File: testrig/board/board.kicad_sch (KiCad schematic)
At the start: 25 parts, among them J1 Conn_01x02_Male, SW1 SW_DIP_x04, U1 AMS1117-3.3, U2 XO2-DIP20, U3 74LVC574, U4 74LVC574, U5 74LVC574, U6 74LVC574, U7 74LVC574, U99 ZIF-40, X1 ASE-80MHz

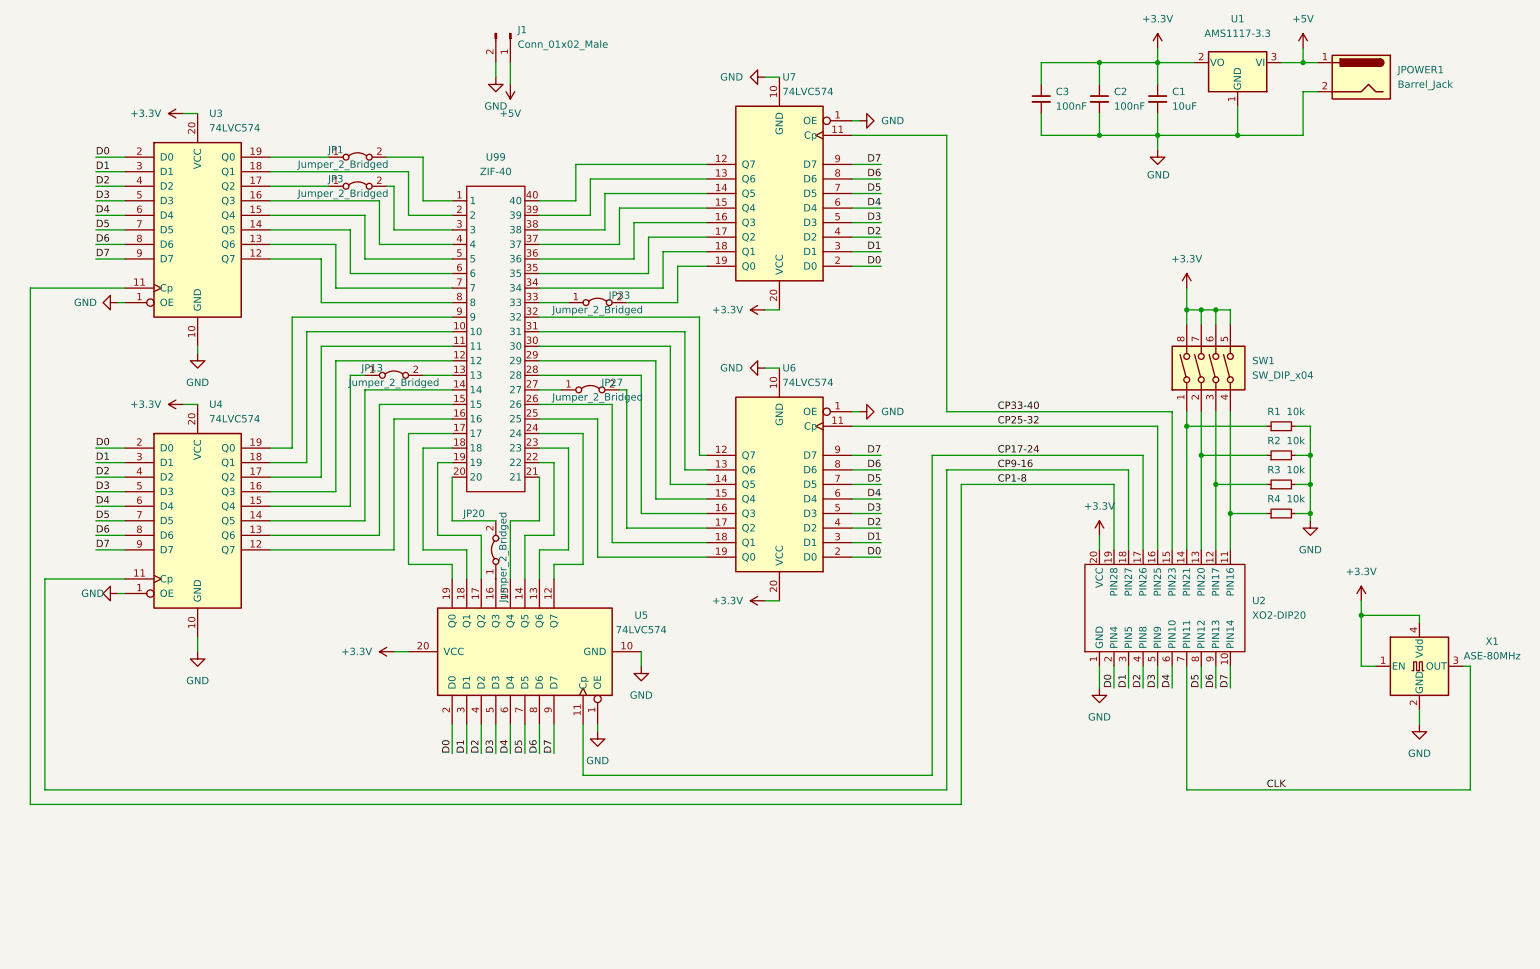
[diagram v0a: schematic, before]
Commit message: Test rig example code
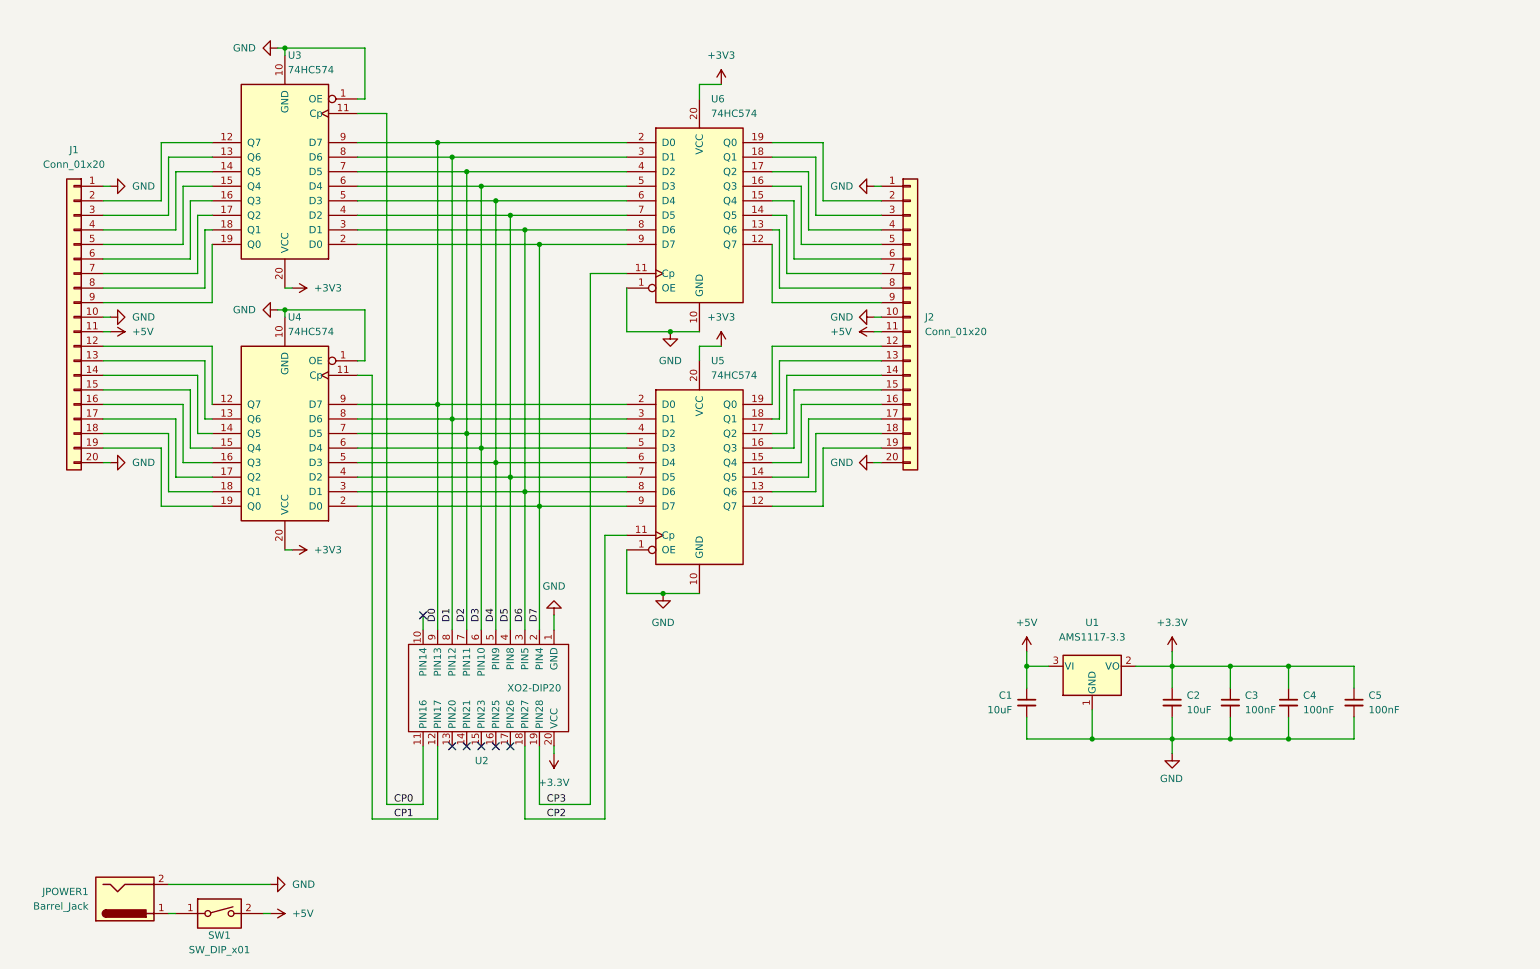
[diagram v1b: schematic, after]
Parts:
- removed J1: Conn_01x02_Male, symbol Connector:Conn_01x02_Male
- removed JP1, JP13, JP20, JP27, JP3, JP33: Jumper_2_Bridged, symbol Jumper:Jumper_2_Bridged
- removed R1, R2, R3, R4: 10k, symbol Device:R_Small
- removed SW1: SW_DIP_x04, symbol Switch:SW_DIP_x04
- removed U3, U4, U5, U6, U7: 74LVC574, symbol 74xx:74LS574
- removed U99: ZIF-40, symbol Library:ZIF-40
- removed X1: ASE-80MHz, Oscillator:Oscillator_SMD_Abracon_ASE-4Pin_3.2x2.5mm, symbol Oscillator:ASE-xxxMHz
- added C2: 10uF, symbol Device:C_Small
- added C5: 100nF, symbol Device:C_Small
- added J1, J2: Conn_01x20, symbol Connector_Generic:Conn_01x20
- added SW1: SW_DIP_x01, symbol Switch:SW_DIP_x01
- added U3, U4, U5, U6: 74HC574, symbol 74xx:74HCT574
- renumbered C2 to C3, C3 to C4
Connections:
- net CLK is gone; now on net D2: U2.7 (PIN11)
- net +3.3V: now also C2.1, C5.1; no longer C1.1
- net +5V: now also C1.1, J1.11 (Pin_11), J2.11 (Pin_11), SW1.2; no longer JPOWER1.1
- net D0: now also U2.9 (PIN13), U3.9 (D7), U4.9 (D7), U5.2 (D0), U6.2 (D0); no longer U2.2 (PIN4)
- net D1: now also U2.8 (PIN12), U3.8 (D6), U4.8 (D6), U5.3 (D1), U6.3 (D1); no longer U2.3 (PIN5)
- net D2: now also U3.7 (D5), U4.7 (D5), U5.4 (D2), U6.4 (D2); no longer U2.4 (PIN8)
- net D3: now also U2.6 (PIN10), U3.6 (D4), U4.6 (D4), U5.5 (D3), U6.5 (D3); no longer U2.5 (PIN9)
- net D4: now also U2.5 (PIN9), U3.5 (D3), U4.5 (D3), U5.6 (D4), U6.6 (D4); no longer U2.6 (PIN10)
- net D5: now also U2.4 (PIN8), U3.4 (D2), U4.4 (D2), U5.7 (D5), U6.7 (D5); no longer U2.8 (PIN12)
- net D6: now also U2.3 (PIN5), U3.3 (D1), U4.3 (D1), U5.8 (D6), U6.8 (D6); no longer U2.9 (PIN13)
- net D7: now also U2.2 (PIN4), U3.2 (D0), U4.2 (D0), U5.9 (D7), U6.9 (D7); no longer U2.10 (PIN14)
- net GND: now also C2.2, C5.2, J1.1 (Pin_1), J1.10 (Pin_10), J1.20 (Pin_20), J2.1 (Pin_1), J2.10 (Pin_10), J2.20 (Pin_20), U3.1 (OE), U3.10 (GND), U4.1 (OE), U4.10 (GND), U5.1 (OE), U5.10 (GND), U6.1 (OE), U6.10 (GND)
- net CP0: now reaches U2.11 (PIN16)
- net CP0: now also U3.11 (Cp)
- net CP1: now reaches U2.12 (PIN17)
- net CP1: now also U4.11 (Cp)
- net CP1-8 renamed CP3
- net CP3: now also U6.11 (Cp)
- net CP17-24: no longer names the net of U2.17 (PIN26)
- net CP25-32: no longer names the net of U2.16 (PIN25)
- net CP33-40: no longer names the net of U2.15 (PIN23)
- net CP9-16 renamed CP2
- net CP2: now also U5.11 (Cp)
- new net: J1.2 (Pin_2), U3.12 (Q7)
- new net: J1.3 (Pin_3), U3.13 (Q6)
- new net: J1.4 (Pin_4), U3.14 (Q5)
- new net: J1.5 (Pin_5), U3.15 (Q4)
- new net: J1.6 (Pin_6), U3.16 (Q3)
- new net: J1.7 (Pin_7), U3.17 (Q2)
- new net: J1.8 (Pin_8), U3.18 (Q1)
- new net: J1.9 (Pin_9), U3.19 (Q0)
- new net: J2.19 (Pin_19), U5.12 (Q7)
- new net: J2.18 (Pin_18), U5.13 (Q6)
- new net: J2.17 (Pin_17), U5.14 (Q5)
- new net: J2.16 (Pin_16), U5.15 (Q4)
- new net: J2.15 (Pin_15), U5.16 (Q3)
- new net: J2.14 (Pin_14), U5.17 (Q2)
- new net: J2.13 (Pin_13), U5.18 (Q1)
- new net: J2.12 (Pin_12), U5.19 (Q0)
- new net: J2.2 (Pin_2), U6.19 (Q0)
- new net: J2.3 (Pin_3), U6.18 (Q1)
- new net: J2.4 (Pin_4), U6.17 (Q2)
- new net: J2.5 (Pin_5), U6.16 (Q3)
- new net: J2.6 (Pin_6), U6.15 (Q4)
- new net: J2.7 (Pin_7), U6.14 (Q5)
- new net: J2.8 (Pin_8), U6.13 (Q6)
- new net: J2.9 (Pin_9), U6.12 (Q7)
- new net: JPOWER1.1, SW1.1
- new net: J1.12 (Pin_12), U4.12 (Q7)
- new net: J1.13 (Pin_13), U4.13 (Q6)
- new net: J1.14 (Pin_14), U4.14 (Q5)
- new net: J1.15 (Pin_15), U4.15 (Q4)
- new net: J1.16 (Pin_16), U4.16 (Q3)
- new net: J1.17 (Pin_17), U4.17 (Q2)
- new net: J1.18 (Pin_18), U4.18 (Q1)
- new net: J1.19 (Pin_19), U4.19 (Q0)
- new net +3V3: U3.20 (VCC), U4.20 (VCC), U5.20 (VCC), U6.20 (VCC)
- no-connect marks 0 -> 6
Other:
- moved on the sheet: C1, C3, C4, JPOWER1, U1, U2

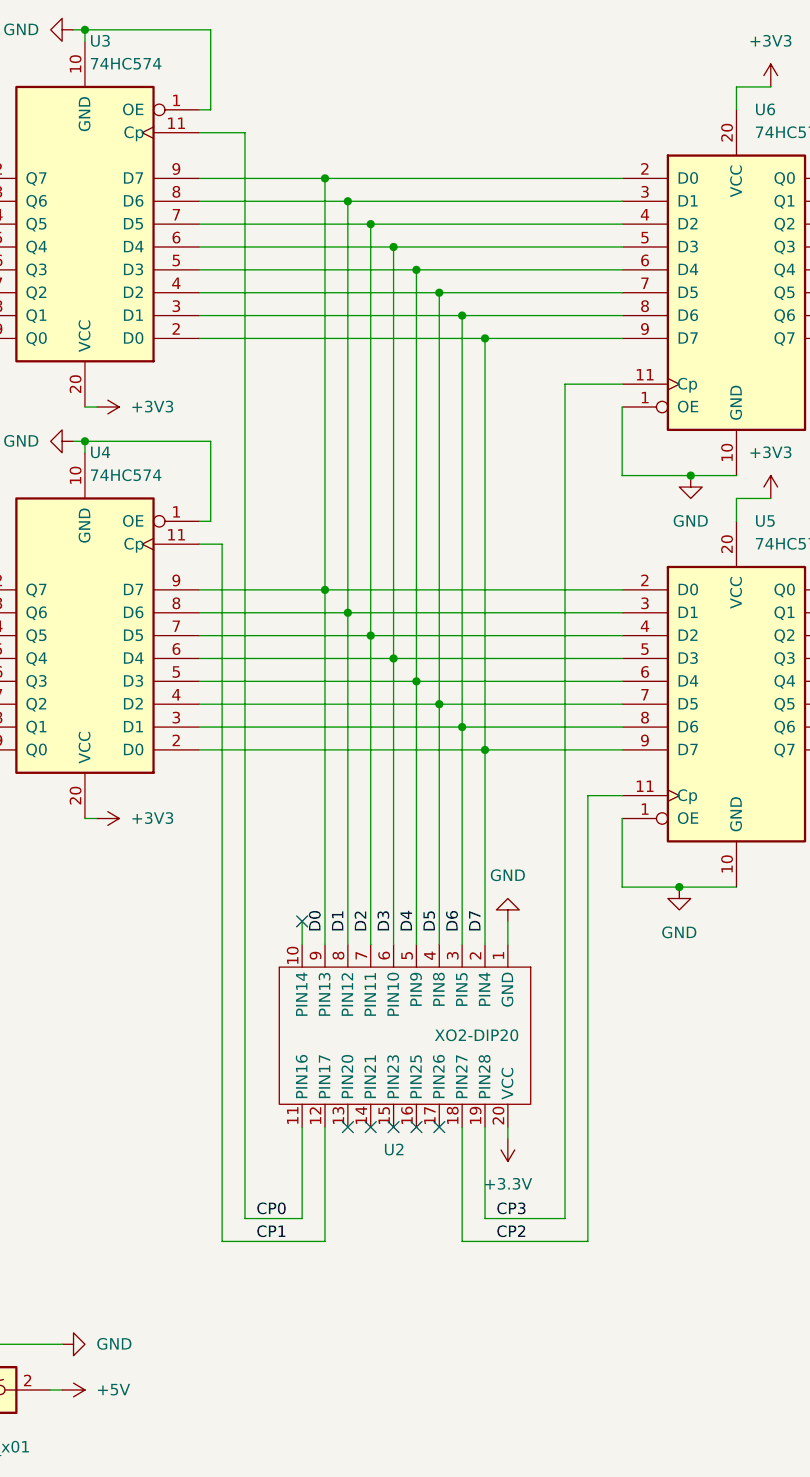
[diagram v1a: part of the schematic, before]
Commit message: Use crystal oscillator instead of internal oscillator
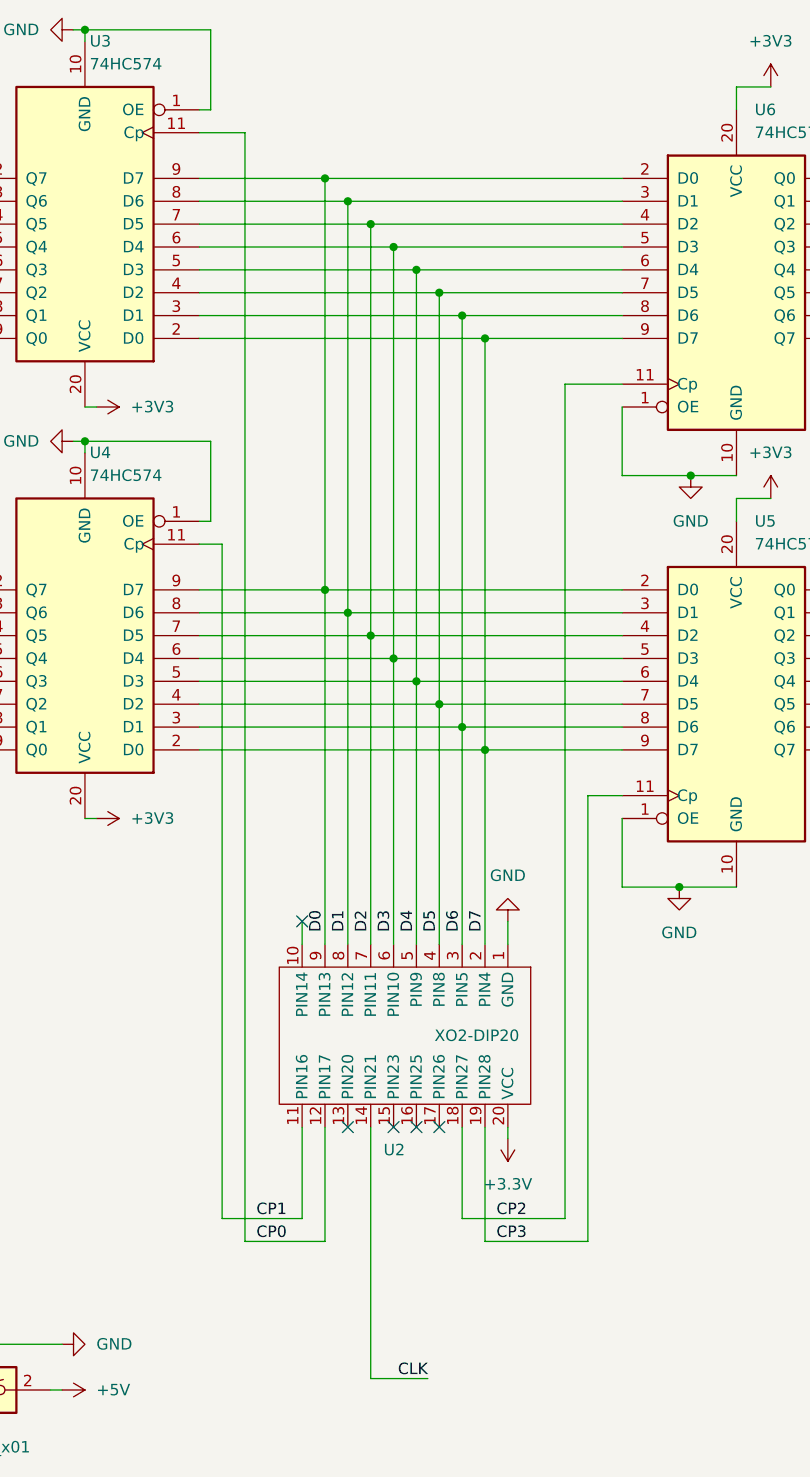
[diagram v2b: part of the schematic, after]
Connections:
- net CP0: now also U2.12 (PIN17); no longer U2.11 (PIN16)
- net CP1: now also U2.11 (PIN16); no longer U2.12 (PIN17)
- net CP2: now also U6.11 (Cp); no longer U5.11 (Cp)
- net CP3: now also U5.11 (Cp); no longer U6.11 (Cp)
- net CLK: now reaches U2.14 (PIN21)
- no-connect marks 6 -> 5
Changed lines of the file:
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@@
   (no_connect (at 99.06 151.13))
   (no_connect (at 101.6 151.13))
-  (no_connect (at 96.52 151.13))
   (no_connect (at 104.14 151.13))
   (wire (pts (xy 104.14 58.42) (xy 124.46 58.42))
@@
     (stroke (width 0) (type default) (color 0 0 0 0))
   )
+  (wire (pts (xy 109.22 163.83) (xy 120.65 163.83))
+    (stroke (width 0) (type default) (color 0 0 0 0))
+  )
   (wire (pts (xy 149.86 96.52) (xy 152.4 96.52))
     (stroke (width 0) (type default) (color 0 0 0 0))
@@
     (stroke (width 0) (type default) (color 0 0 0 0))
   )
+  (wire (pts (xy 80.01 161.29) (xy 80.01 86.36))
+    (stroke (width 0) (type default) (color 0 0 0 0))
+  )
   (wire (pts (xy 168.91 53.34) (xy 167.64 53.34))
     (stroke (width 0) (type default) (color 0 0 0 0))
@@
     (stroke (width 0) (type default) (color 0 0 0 0))
   )
+  (wire (pts (xy 96.52 179.07) (xy 102.87 179.07))
+    (stroke (width 0) (type default) (color 0 0 0 0))
+  )
   (wire (pts (xy 149.86 50.8) (xy 156.21 50.8))
     (stroke (width 0) (type default) (color 0 0 0 0))
@@
     (stroke (width 0) (type default) (color 0 0 0 0))
   )
+  (wire (pts (xy 82.55 163.83) (xy 91.44 163.83))
+    (stroke (width 0) (type default) (color 0 0 0 0))
+  )
   (wire (pts (xy 229.87 149.86) (xy 219.71 149.86))
     (stroke (width 0) (type default) (color 0 0 0 0))
@@
     (stroke (width 0) (type default) (color 0 0 0 0))
   )
-  (wire (pts (xy 109.22 161.29) (xy 118.11 161.29))
-    (stroke (width 0) (type default) (color 0 0 0 0))
-  )
-  (wire (pts (xy 109.22 151.13) (xy 109.22 161.29))
+  (wire (pts (xy 106.68 161.29) (xy 118.11 161.29))
+    (stroke (width 0) (type default) (color 0 0 0 0))
+  )
+  (wire (pts (xy 109.22 151.13) (xy 109.22 163.83))
     (stroke (width 0) (type default) (color 0 0 0 0))
   )
@@
     (stroke (width 0) (type default) (color 0 0 0 0))
   )
-  (wire (pts (xy 80.01 163.83) (xy 80.01 86.36))
-    (stroke (width 0) (type default) (color 0 0 0 0))
-  )
   (wire (pts (xy 149.86 106.68) (xy 157.48 106.68))
     (stroke (width 0) (type default) (color 0 0 0 0))
@@
     (stroke (width 0) (type default) (color 0 0 0 0))
   )
-  (wire (pts (xy 80.01 163.83) (xy 91.44 163.83))
-    (stroke (width 0) (type default) (color 0 0 0 0))
-  )
   (wire (pts (xy 49.53 86.36) (xy 33.02 86.36))
     (stroke (width 0) (type default) (color 0 0 0 0))
@@
     (stroke (width 0) (type default) (color 0 0 0 0))
   )
-  (wire (pts (xy 82.55 161.29) (xy 82.55 40.64))
+  (wire (pts (xy 82.55 40.64) (xy 82.55 163.83))
     (stroke (width 0) (type default) (color 0 0 0 0))
   )
@@
     (stroke (width 0) (type default) (color 0 0 0 0))
   )
-  (wire (pts (xy 88.9 161.29) (xy 82.55 161.29))
+  (wire (pts (xy 80.01 161.29) (xy 88.9 161.29))
     (stroke (width 0) (type default) (color 0 0 0 0))
   )
@@
     (stroke (width 0) (type default) (color 0 0 0 0))
   )
-  (wire (pts (xy 106.68 163.83) (xy 120.65 163.83))
-    (stroke (width 0) (type default) (color 0 0 0 0))
-  )
   (wire (pts (xy 194.31 137.16) (xy 194.31 140.97))
     (stroke (width 0) (type default) (color 0 0 0 0))
@@
     (stroke (width 0) (type default) (color 0 0 0 0))
   )
+  (wire (pts (xy 96.52 151.13) (xy 96.52 179.07))
+    (stroke (width 0) (type default) (color 0 0 0 0))
+  )
   (wire (pts (xy 130.81 124.46) (xy 137.16 124.46))
     (stroke (width 0) (type default) (color 0 0 0 0))
@@
     (stroke (width 0) (type default) (color 0 0 0 0))
   )
-  (wire (pts (xy 106.68 151.13) (xy 106.68 163.83))
+  (wire (pts (xy 106.68 151.13) (xy 106.68 161.29))
     (stroke (width 0) (type default) (color 0 0 0 0))
   )
@@
     (effects (font (size 1.27 1.27)) (justify right bottom))
   )
-  (label "CP3" (at 110.49 161.29 0)
+  (label "CP2" (at 110.49 161.29 0)
     (effects (font (size 1.27 1.27)) (justify left bottom))
   )
@@
     (effects (font (size 1.27 1.27)) (justify right bottom))
   )
-  (label "CP2" (at 110.49 163.83 0)
+  (label "CP3" (at 110.49 163.83 0)
     (effects (font (size 1.27 1.27)) (justify left bottom))
   )
+  (label "CLK" (at 102.87 179.07 180)
+    (effects (font (size 1.27 1.27)) (justify right bottom))
+  )
   (label "D7" (at 109.22 127 270)
     (effects (font (size 1.27 1.27)) (justify right bottom))
@@
     (effects (font (size 1.27 1.27)) (justify right bottom))
   )
-  (label "CP0" (at 83.82 161.29 0)
+  (label "CP1" (at 83.82 161.29 0)
     (effects (font (size 1.27 1.27)) (justify left bottom))
   )
@@
     (effects (font (size 1.27 1.27)) (justify right bottom))
   )
-  (label "CP1" (at 83.82 163.83 0)
+  (label "CP0" (at 83.82 163.83 0)
     (effects (font (size 1.27 1.27)) (justify left bottom))
   )
